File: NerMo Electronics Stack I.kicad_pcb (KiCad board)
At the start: 2 copper layers, 83 x 66.4 mm, 80 parts, among them J1 PWM 5, J10 PWM 8, J11 PWM 9, J12 PWM 10, J13 PWM 11, J14 PWM 12, J15 PWM 13, J16 PWM 14, J17 PWM 15, J18 PWM 16, J2 Raspberry_Pi_Zero, J20 VBAT_IN, J3 PWM 1, J4 Address_Sel, J5 PWM 2, J6 PWM 3, J7 PWM 4, J8 PWM 6, J9 PWM 7, Q1 IRF7404, SW1 SW_SPDT, U3 AMS1117-3.3, U5 PCA9685PW, U6 INA3221

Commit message: feat: NerMo Stack V1
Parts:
- removed the *REF at (112.7, 85.4)
- removed the *REF at (112.7, 62.4)
- removed the *REF at (54.7, 85.4)
- removed C4: 10uF, Capacitor_SMD:C_0603_1608Metric
- removed J1: PWM 5, Connector_Molex:Molex_PicoBlade_53261-0371_1x03-1MP_P1.25mm_Horizontal
- removed J10: PWM 8, Connector_Molex:Molex_PicoBlade_53261-0371_1x03-1MP_P1.25mm_Horizontal
- removed J11: PWM 9, Connector_Molex:Molex_PicoBlade_53261-0371_1x03-1MP_P1.25mm_Horizontal
- removed J12: PWM 10, Connector_Molex:Molex_PicoBlade_53261-0371_1x03-1MP_P1.25mm_Horizontal
- removed J13: PWM 11, Connector_Molex:Molex_PicoBlade_53261-0371_1x03-1MP_P1.25mm_Horizontal
- removed J14: PWM 12, Connector_Molex:Molex_PicoBlade_53261-0371_1x03-1MP_P1.25mm_Horizontal
- removed J15: PWM 13, Connector_Molex:Molex_PicoBlade_53261-0371_1x03-1MP_P1.25mm_Horizontal
- removed J16: PWM 14, Connector_Molex:Molex_PicoBlade_53261-0371_1x03-1MP_P1.25mm_Horizontal
- removed J17: PWM 15, Connector_Molex:Molex_PicoBlade_53261-0371_1x03-1MP_P1.25mm_Horizontal
- removed J18: PWM 16, Connector_Molex:Molex_PicoBlade_53261-0371_1x03-1MP_P1.25mm_Horizontal
- removed J5: PWM 2, Connector_Molex:Molex_PicoBlade_53261-0371_1x03-1MP_P1.25mm_Horizontal
- removed J6: PWM 3, Connector_Molex:Molex_PicoBlade_53261-0371_1x03-1MP_P1.25mm_Horizontal
- removed J7: PWM 4, Connector_Molex:Molex_PicoBlade_53261-0371_1x03-1MP_P1.25mm_Horizontal
- removed J8: PWM 6, Connector_Molex:Molex_PicoBlade_53261-0371_1x03-1MP_P1.25mm_Horizontal
- removed J9: PWM 7, Connector_Molex:Molex_PicoBlade_53261-0371_1x03-1MP_P1.25mm_Horizontal
- removed JP3: Addr0, Jumper:SolderJumper-2_P1.3mm_Open_TrianglePad1.0x1.5mm
- removed JP4: Addr1, Jumper:SolderJumper-2_P1.3mm_Open_TrianglePad1.0x1.5mm
- removed JP5: Addr2, Jumper:SolderJumper-2_P1.3mm_Open_TrianglePad1.0x1.5mm
- removed JP6: Addr3, Jumper:SolderJumper-2_P1.3mm_Open_TrianglePad1.0x1.5mm
- removed JP7: Addr4, Jumper:SolderJumper-2_P1.3mm_Open_TrianglePad1.0x1.5mm
- removed JP8: Addr5, Jumper:SolderJumper-2_P1.3mm_Open_TrianglePad1.0x1.5mm
- removed R11: 4k7, Resistor_SMD:R_0805_2012Metric
- removed R12, R13, R14, R15, R16, R17, R18: 10k, Resistor_SMD:R_0603_1608Metric
- removed REF**: PinHeader_1x04_P2.54mm_Vertical, Connector_PinHeader_2.54mm:PinHeader_1x04_P2.54mm_Vertical
- removed REF**: PinHeader_1x06_P2.54mm_Vertical, Connector_PinHeader_2.54mm:PinHeader_1x06_P2.54mm_Vertical
- removed REF**: MountingHole_2.5mm_Pad, MountingHole:MountingHole_2.5mm_Pad
- removed REF**: PinSocket_1x04_P2.54mm_Vertical, Connector_PinSocket_2.54mm:PinSocket_1x04_P2.54mm_Vertical
- removed REF**: PinSocket_1x06_P2.54mm_Vertical, Connector_PinSocket_2.54mm:PinSocket_1x06_P2.54mm_Vertical
- removed RN1, RN2, RN3, RN4: 220, Resistor_SMD:R_Array_Concave_4x0603
- removed U5: PCA9685PW, Package_SO:TSSOP-28_4.4x9.7mm_P0.65mm
- added *REF: , , F.Cu at (100.0, 88.5)
- added *REF: , , F.Cu at (86.0, 103.5)
- added *REF: , , F.Cu at (71.5, 88.5)
- added *REF: , , F.Cu at (129.5, 111.5)
- added *REF: , , F.Cu at (129.5, 88.5)
- added *REF: , , F.Cu at (71.5, 111.5)
- added *REF: , , F.Cu at (128.5, 103.5)
- added C1: 2.2uF, Capacitor_SMD:C_0805_2012Metric, B.Cu at (66.6, 93.7)
- added C2: 0.1uF, Capacitor_SMD:C_0805_2012Metric, B.Cu at (66.6, 98.7)
- added D4: LED, LED_SMD:LED_0805_2012Metric_Pad1.15x1.40mm_HandSolder, F.Cu at (133.8, 93.0)
- added R8: 3k, Resistor_SMD:R_0805_2012Metric, F.Cu at (130.7, 93.2)
- added U1: MPU-6050, Sensor_Motion:InvenSense_QFN-24_4x4mm_P0.5mm, B.Cu at (71.4, 99.9)
- C5, R3, R5, R6, R7, R9, SW1: moved to F.Cu
- J2: footprint Custom_Modules:Raspberry_Pi_Zero_2_W_Underside_LowProfile -> Custom_Modules:Raspberry_Pi_Zero_2_W_HDR-TH
- J3: value PWM 1 -> Conn_02x06_Odd_Even; footprint Connector_JST:JST_SH_SM03B-SRSS-TB_1x03-1MP_P1.00mm_Horizontal -> Connector_PinSocket_1.27mm:PinSocket_2x06_P1.27mm_Vertical
- U2: footprint Connector_PinHeader_2.54mm:PinHeader_1x05_P2.54mm_Vertical_SMD_Pin1Left -> Connector_PinHeader_2.54mm:PinHeader_1x05_P2.54mm_Vertical
- moved R38 60.4 mm to (117.4, 106.2), turned to 90 degrees
- moved R1 60.0 mm to (123.4, 88.4)
- moved R39 58.4 mm to (119.8, 101.5)
- moved R43 55.1 mm to (115.5, 106.2), turned to -90 degrees
- moved R2 54.8 mm to (119.1, 88.4)
- moved R40 52.5 mm to (112.1, 105.8), turned to -90 degrees
- moved U6 50.5 mm to (113.5, 101.2)
- moved C5 47.1 mm to (70.4, 104.5), turned to 90 degrees
- moved R44 46.7 mm to (109.3, 103.5), turned to -90 degrees
- moved U2 46.2 mm to (90.9, 85.9), turned to 90 degrees
- moved R41 45.6 mm to (93.0, 106.6), turned to 0 degrees
- moved R42 44.7 mm to (96.4, 106.6)
- moved R36 43.3 mm to (113.8, 97.2), turned to 0 degrees
- moved R45 42.0 mm to (108.7, 99.2)
- moved SW1 38.6 mm to (121.8, 84.3), turned to 180 degrees
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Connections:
- C5 pad 1: +3.3V -> +6V
- J20 pad 1: BAT_GND -> GND
- J3 pad 1: Net-(J3-Pin_1) -> /I2C_SCL
- J3 pad 2: +6V -> /I2C_SDA
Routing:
- net +3.3V: track 0.00 -> 168.3 mm, vias 0 -> 10
- net /I2C_SCL: track 0.00 -> 94.5 mm, vias 0 -> 5
- net /I2C_SDA: track 0.00 -> 90.7 mm, vias 0 -> 3
- net +5V: track 0.00 -> 87.6 mm, vias 0 -> 10
- net +5V_PWR: track 0.00 -> 53.0 mm, vias 0 -> 8
- net +6V: track 0.00 -> 47.4 mm, vias 0 -> 11
- net +3.3V_PWR: track 0.00 -> 22.4 mm, vias 0 -> 2
- net Net-(Q1-G): track 0.00 -> 15.4 mm
- net GND: track 0.00 -> 12.4 mm, vias 0 -> 56
- net Net-(U6-PV): track 0.00 -> 12.3 mm, vias 0 -> 2
- net VBAT: track 0.00 -> 11.6 mm, vias 0 -> 15
- net Net-(U1-CPOUT): track 0.00 -> 10.8 mm, vias 0 -> 2
- net /IMU1_I2C_Sel: track 0.00 -> 10.1 mm
- net Net-(U6-VPU): track 0.00 -> 7.56 mm
- net VBAT_IN: track 0.00 -> 5.42 mm
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- added copper zone on B.Cu, net +3.3V_PWR
- added copper zone on B.Cu, net +5V
- added copper zone on F.Cu, net +5V
- added copper zone on B.Cu, net +5V_PWR
- added copper zone on F.Cu, net +5V_PWR
- added copper zone on B.Cu, net +6V
- added copper zone on F.Cu, net +6V
- added copper zone on B.Cu, net +6V_PWR
- added copper zone on F.Cu, net +6V_PWR
- added copper zone on B.Cu, net GND
- added copper zone on F.Cu, net GND
- added copper zone on B.Cu, net VBAT
- added copper zone on F.Cu, net VBAT
- added copper zone on B.Cu, net VBAT_IN
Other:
- board size 83 x 66.4 mm -> 74 x 36 mm
- board text added: "3A"
- board text added: "3V3"
- board text added: "3V3 1A LDO"
- board text added: "5A"
- board text added: "5V"
- board text added: "6V"
- board text added: "BAT"
- board text added: "INA3221 PMON"
- board text added: "MAX"
- board text added: "NerMo Electronics Stack I"
- board text added: "OUT"
- board text removed: "Connector Board"
- board text removed: "Mechanical Mockup! Layout not final no wiring / silkscreen"
- board text removed: "NerMo EPS V0.1 Preview"
- board text removed: "PWR IN"
- board text removed: "PWR Light"
- board text removed: "Tail"

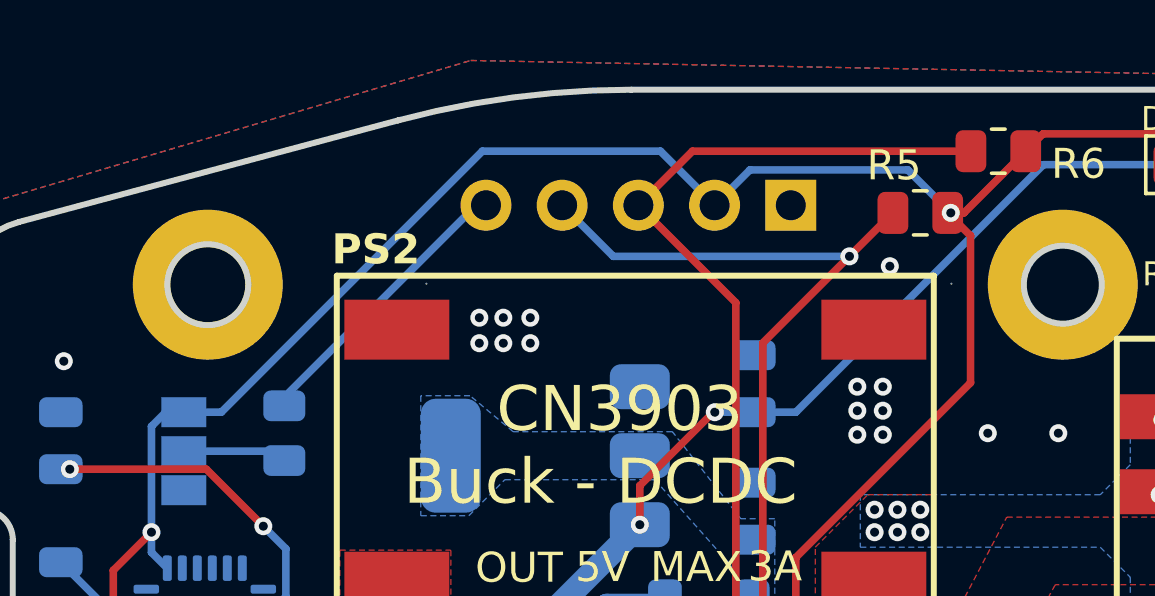
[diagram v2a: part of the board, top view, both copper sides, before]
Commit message: fix: fixed external IMU Connector positioning
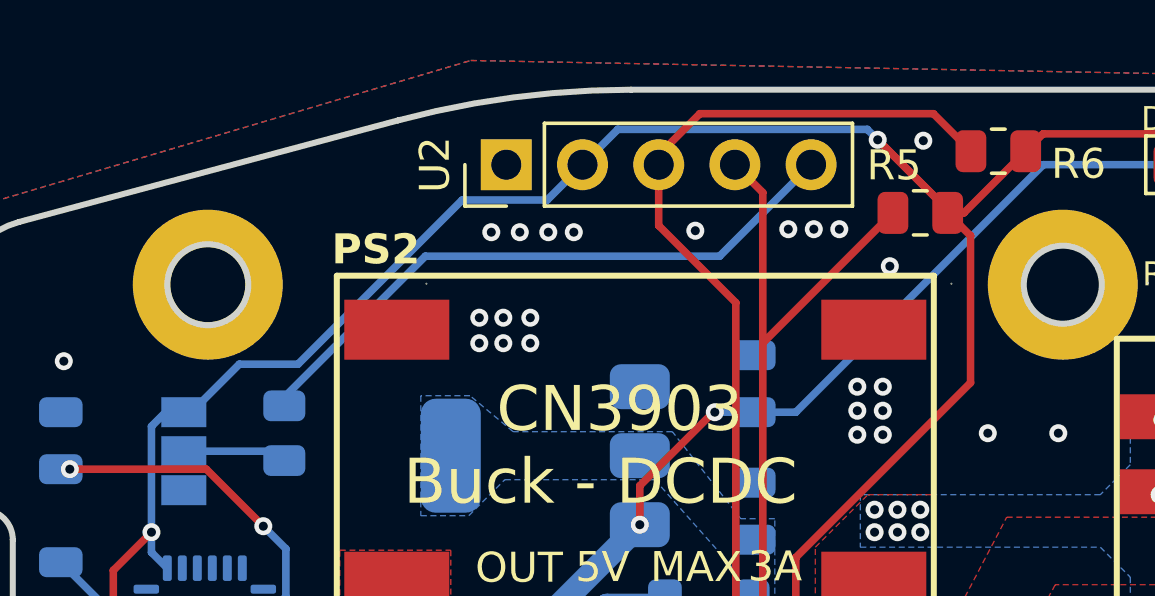
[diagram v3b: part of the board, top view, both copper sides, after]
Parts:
- U2: moved to F.Cu
- moved U2 9.58 mm to (81.5, 84.5)
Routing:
- net /IMU1_I2C_Sel: track 10.1 -> 21.5 mm
- net /I2C_SCL: track 94.5 -> 90.5 mm, vias 5 -> 4
- net +3.3V: track 168.3 -> 171.3 mm
- net /I2C_SDA: track 90.7 -> 91.8 mm
- net GND: vias 56 -> 65

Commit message: feat: V0.2
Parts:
- added TP1: 5V Test Point, TestPoint:TestPoint_Pad_2.0x2.0mm, B.Cu at (108.8, 84.0)
- added TP2: 3V3 Test Point, TestPoint:TestPoint_Pad_2.0x2.0mm, B.Cu at (104.7, 84.0)
- added TP3: 6V Test Point, TestPoint:TestPoint_Pad_2.0x2.0mm, B.Cu at (113.2, 84.0)
- added TP4: VBAT Test Point, TestPoint:TestPoint_Pad_2.0x2.0mm, B.Cu at (117.5, 84.0)
- added TP5: GND Test Point, TestPoint:TestPoint_Pad_2.0x2.0mm, B.Cu at (125.9, 84.0)
- moved R2 0.52 mm to (119.7, 88.4)
- moved R1 0.39 mm to (123.0, 88.4)
- moved R4 0.30 mm to (74.3, 93.5)
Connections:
- C5 pad 1: +6V -> +5V
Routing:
- net +6V: track 47.4 -> 23.1 mm, vias 11 -> 7
- net VBAT: track 11.6 -> 18.7 mm
- net /I2C_SCL: track 90.5 -> 85.8 mm
- net /Power Supply/SW_PWR_ON: track 3.80 -> 2.70 mm
- net /IMU1_I2C_Sel: track 21.5 -> 20.6 mm
- net Net-(Q1-G): track 15.4 -> 14.5 mm, vias 0 -> 2
- net Net-(J4-Pin_2): track 3.48 -> 4.08 mm
- net GND: vias 65 -> 57
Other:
- outline, holes or cut-outs redrawn
- board text added: "10"
- board text added: "12"
- board text added: "14"
- board text added: "16"
- board text added: "18"
- board text added: "2"
- board text added: "20"
- board text added: "22"
- board text added: "24"
- board text added: "26"
- board text added: "28"
- board text added: "30"
- board text added: "32"
- board text added: "34"
- board text added: "36"
- board text added: "38"
- board text added: "4"
- board text added: "40"
- board text added: "6"
- board text added: "8"
- board text added: "@space.zhang"
- board text added: "GND"
- board text added: "VBAT"
- board text added: "Ver 0.2"
